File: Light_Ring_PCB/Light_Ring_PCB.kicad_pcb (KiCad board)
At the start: 2 copper layers, 120 x 120 mm, 126 parts, among them J1 LIGHT_OUT, Q1 Q_Photo_NPN, Q10 Q_Photo_NPN, Q11 Q_Photo_NPN, Q12 Q_Photo_NPN, Q13 Q_Photo_NPN, Q14 Q_Photo_NPN, Q15 Q_Photo_NPN, Q16 Q_Photo_NPN, Q17 Q_Photo_NPN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

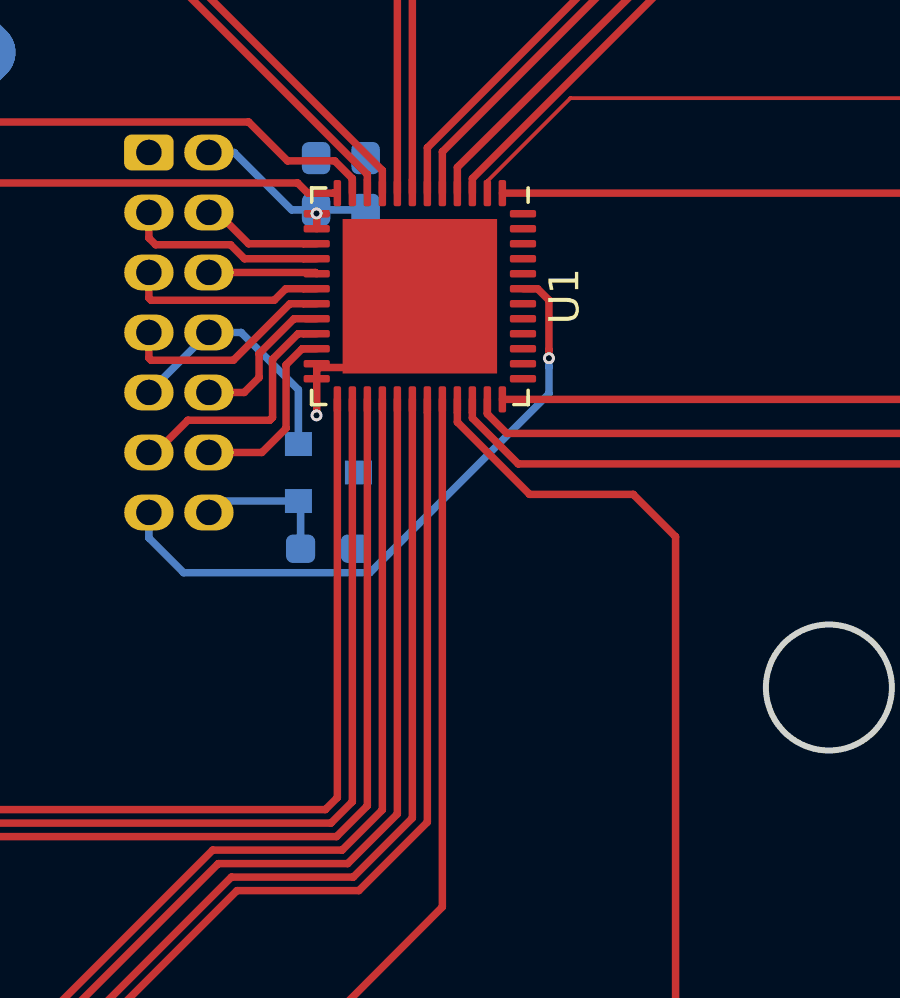
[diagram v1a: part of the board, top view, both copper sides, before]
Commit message: Finished Power Planes and layout, started drawing traces [MAIN BOARD]
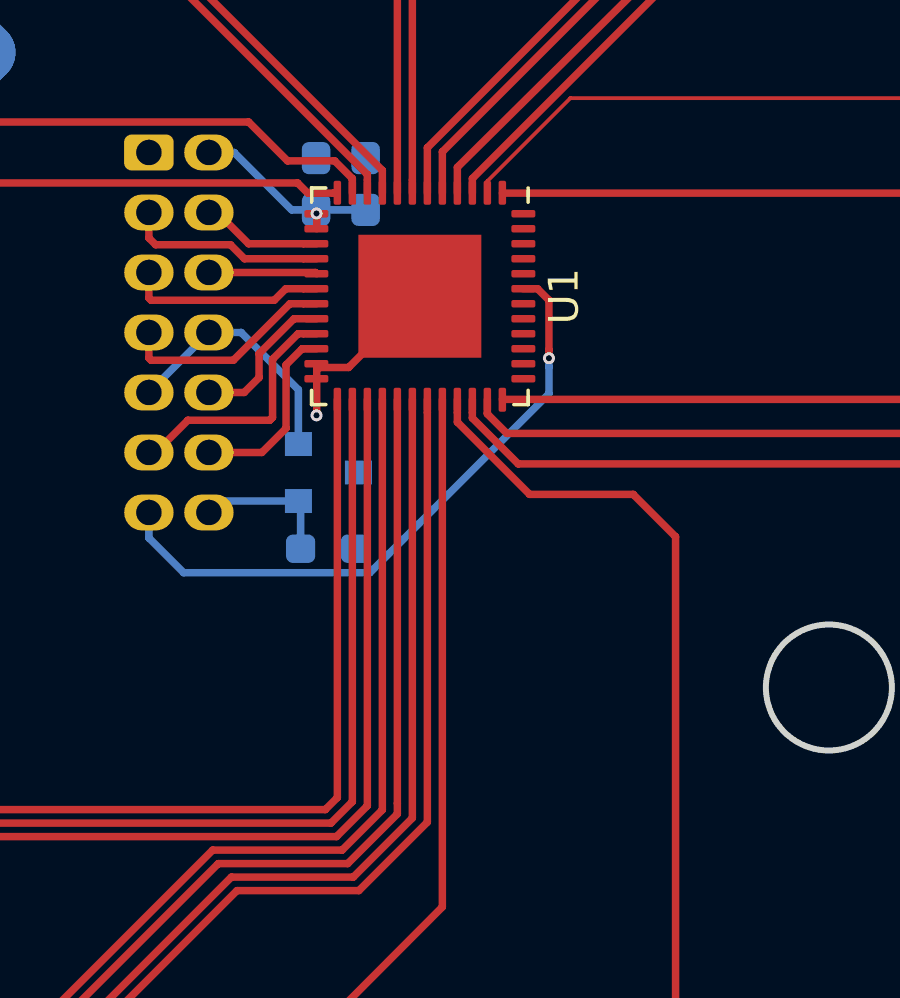
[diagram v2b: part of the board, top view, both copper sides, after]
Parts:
- R1, R10, R11, R12, R17, R18, R19, R2, R20, R25, R26, R27, R28, R3, R33, R34, R37, R38, R4, R41, R42, R45, R46, R9: value 10k -> 6k2
- R13, R14, R15, R16, R21, R22, R23, R24, R29, R30, R31, R32, R35, R36, R39, R40, R43, R44, R47, R48, R5, R6, R7, R8: value 120R -> 12R
- U1: footprint Package_DFN_QFN:QFN-48-1EP_7x7mm_P0.5mm_EP5.15x5.15mm -> Package_CSP:LFCSP-48-1EP_7x7mm_P0.5mm_EP4.1x4.1mm
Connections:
- net +5V renamed +3V3
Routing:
- net +5V: track 0.00 -> 22.6 mm, vias 0 -> 9
- net +3V3: track 29.2 -> 6.53 mm, vias 10 -> 1
- net GND: track 177.0 -> 180.4 mm

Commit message: Updated to Kicad 6
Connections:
- net ~CL renamed ~{CL}
- net ~EN renamed ~{EN}
- net ~WR renamed ~{WR}
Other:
- net class Default removed
- rule pad_to_mask_clearance: 0.051 -> 0
